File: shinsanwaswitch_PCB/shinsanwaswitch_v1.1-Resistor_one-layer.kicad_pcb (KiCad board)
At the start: 2 copper layers, 26.3 x 15.4 mm, 9 parts, among them J1 Conn_01x05_Male, Q1 2SC5395

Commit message: Update for DIY-make boards
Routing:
- net (no net): vias 0 -> 5
- added copper zone on B.Cu, net (none)
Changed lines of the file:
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@@
     (effects (font (size 0.5 0.5) (thickness 0.125)))
   )
+  (via (at 146.1 76.8) (size 2.65) (drill 2.58) (layers "F.Cu" "B.Cu") (free) (net 0))
+  (via (at 149.77 86.2) (size 1.1) (drill 1) (layers "F.Cu" "B.Cu") (free) (net 0))
+  (via (at 137.525 88.7) (size 2.05) (drill 1.98) (layers "F.Cu" "B.Cu") (free) (net 0))
+  (via (at 149.78 88.7) (size 1.5) (drill 1.4) (layers "F.Cu" "B.Cu") (free) (net 0))
+  (via (at 151.1 76.79) (size 2.65) (drill 2.58) (layers "F.Cu" "B.Cu") (free) (net 0))
   (segment (start 151.145 87.325) (end 148.395 87.325) (width 0.7) (layer "B.Cu") (net 1))
   (segment (start 148.395 87.325) (end 147.27 86.2) (width 0.7) (layer "B.Cu") (net 1))
@@
   (segment (start 145.265299 83.541846) (end 147.298694 83.541846) (width 0.8) (layer "B.Cu") (net 8))
   (segment (start 137.47 83.72) (end 133.62 83.72) (width 0.8) (layer "B.Cu") (net 8))
+  (zone (net 0) (net_name "") (layer "B.Cu") (hatch edge 0.508)
+    (connect_pads (clearance 0.508))
+    (min_thickness 0.254) (filled_areas_thickness no)
+    (fill yes (thermal_gap 0.508) (thermal_bridge_width 0.508))
+    (polygon
+      (pts
+        (xy 154.94 90.932)
+        (xy 127 90.932)
+        (xy 127.254 74.422)
+        (xy 154.94 74.422)
+      )
+    )
+  )
 )

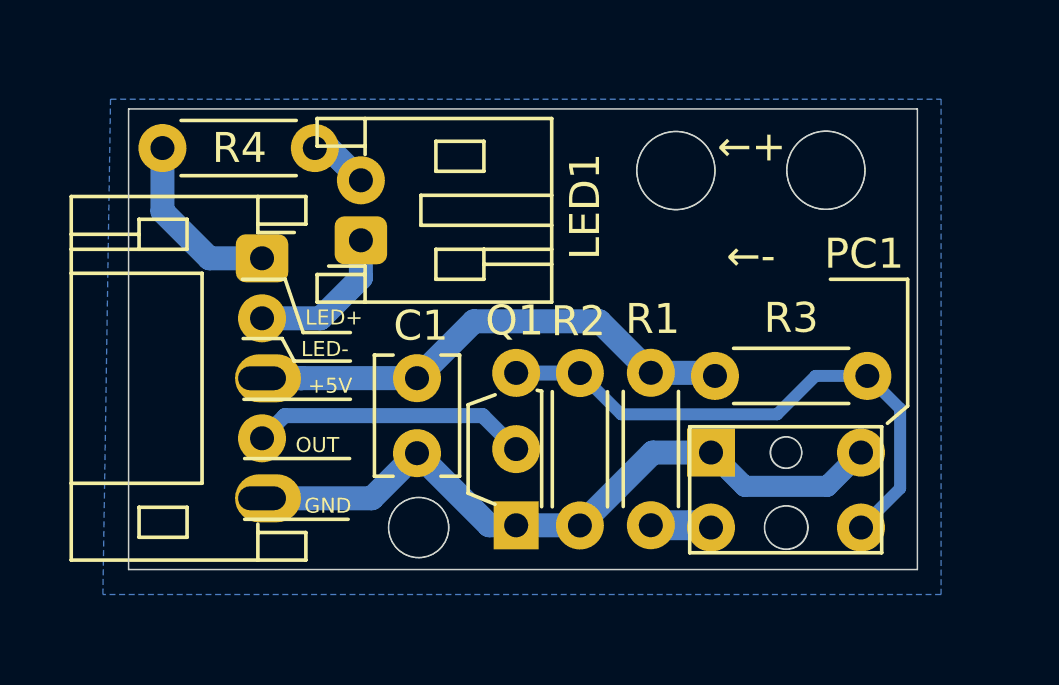
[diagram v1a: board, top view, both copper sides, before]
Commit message: Massive update of DIY-boards to make it easier to print and drill
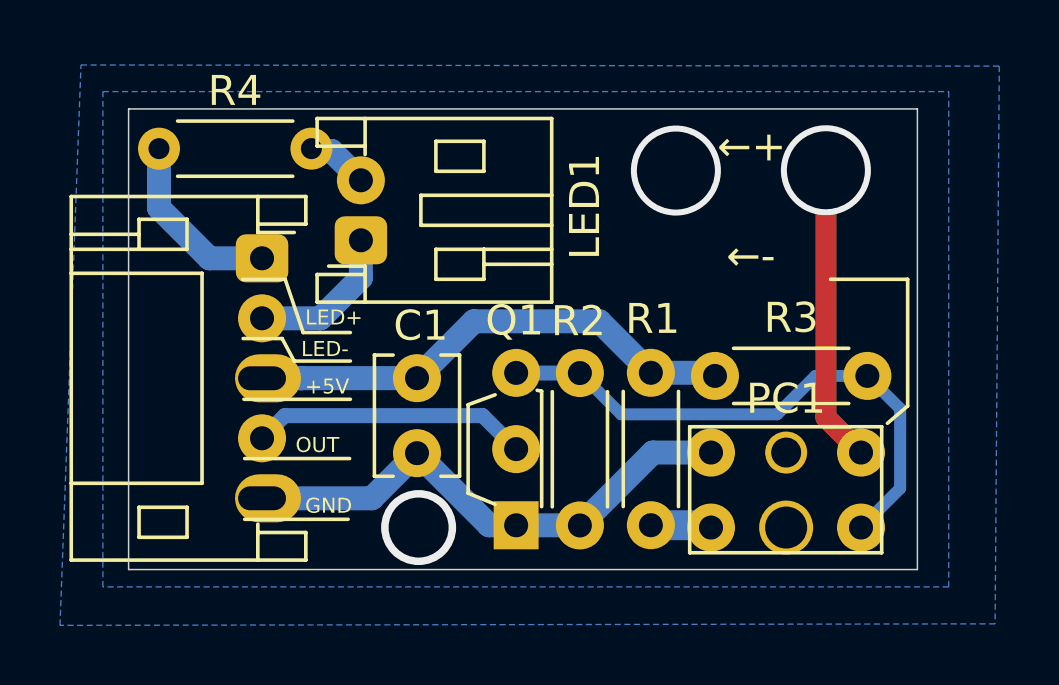
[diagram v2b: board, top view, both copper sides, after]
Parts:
- PC1: footprint RPI-221:RPI-352 -> RPI-221:RPI-352_otherholes
- moved PC1 4.74 mm to (149.8, 86.2)
- moved R4 0.12 mm to (128.9, 76.1)
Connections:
- PC1 pad : (no net) -> GND
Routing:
- net GND: track 23.5 -> 27.5 mm, vias 0 -> 3
- net (no net): vias 5 -> 0
- added copper zone on B.Cu, net GND
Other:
- outline, holes or cut-outs redrawn
- board text added: "SHINSANWASWITCH board by steelpuxnastik / Doctopus from ProjectDIVA.net ver 1.1 with LED driver 2021"
- board text removed: "SHINSANWASWITCH board by steelpuxnastik / Doctopus from ProjectDIVA.net ver 1.1 2021"
